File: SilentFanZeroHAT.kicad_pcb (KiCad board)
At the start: 2 copper layers, 65 x 30 mm, 43 parts, among them J1 24V Input, J2 Fan_0, J3 Fan_1, J4 Fan_2, P1 Conn_02x20_Odd_Even, Q1 AOSS32338C, Q2 AOSS32338C, Q3 AOSS32338C, U1 74LVC1G17, U2 74LVC1G17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

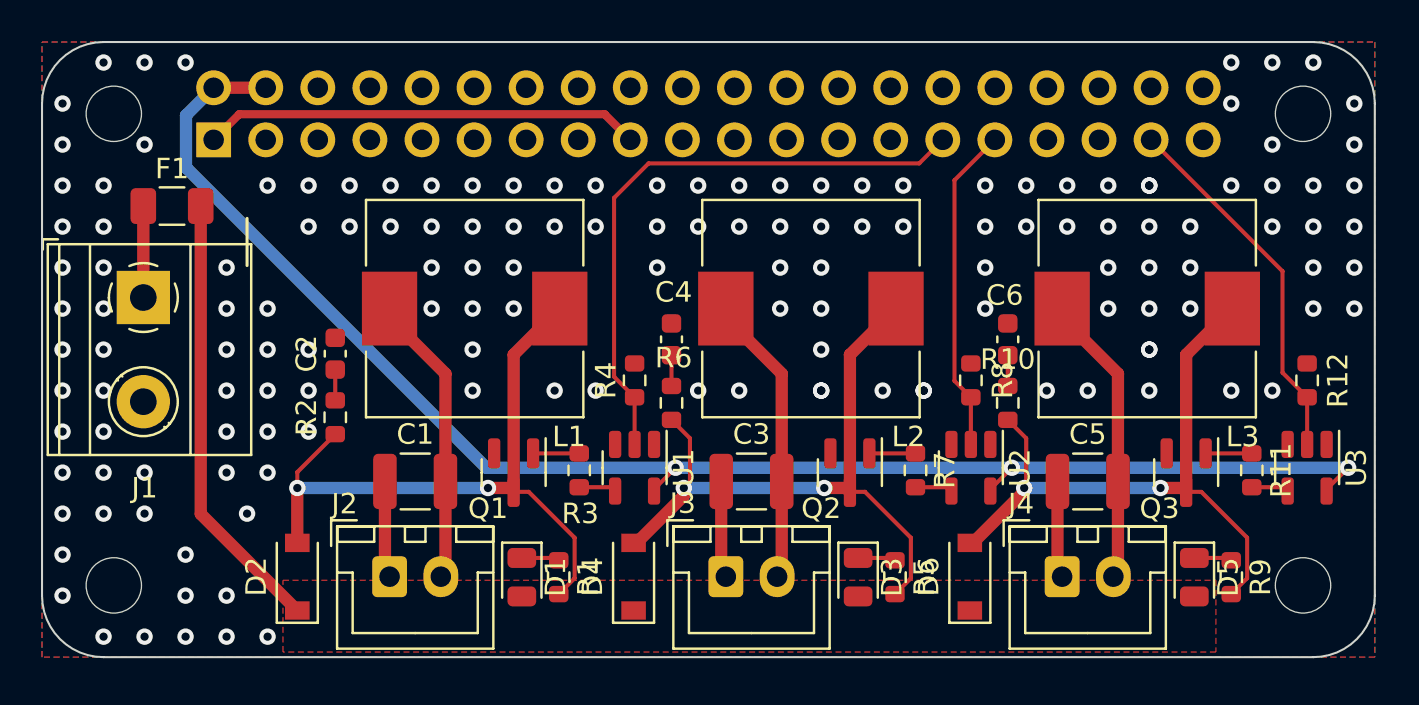
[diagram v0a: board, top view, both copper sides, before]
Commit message: Fixing the silkscreen mess
Thanks Infinite Entropy for alerting me about that.
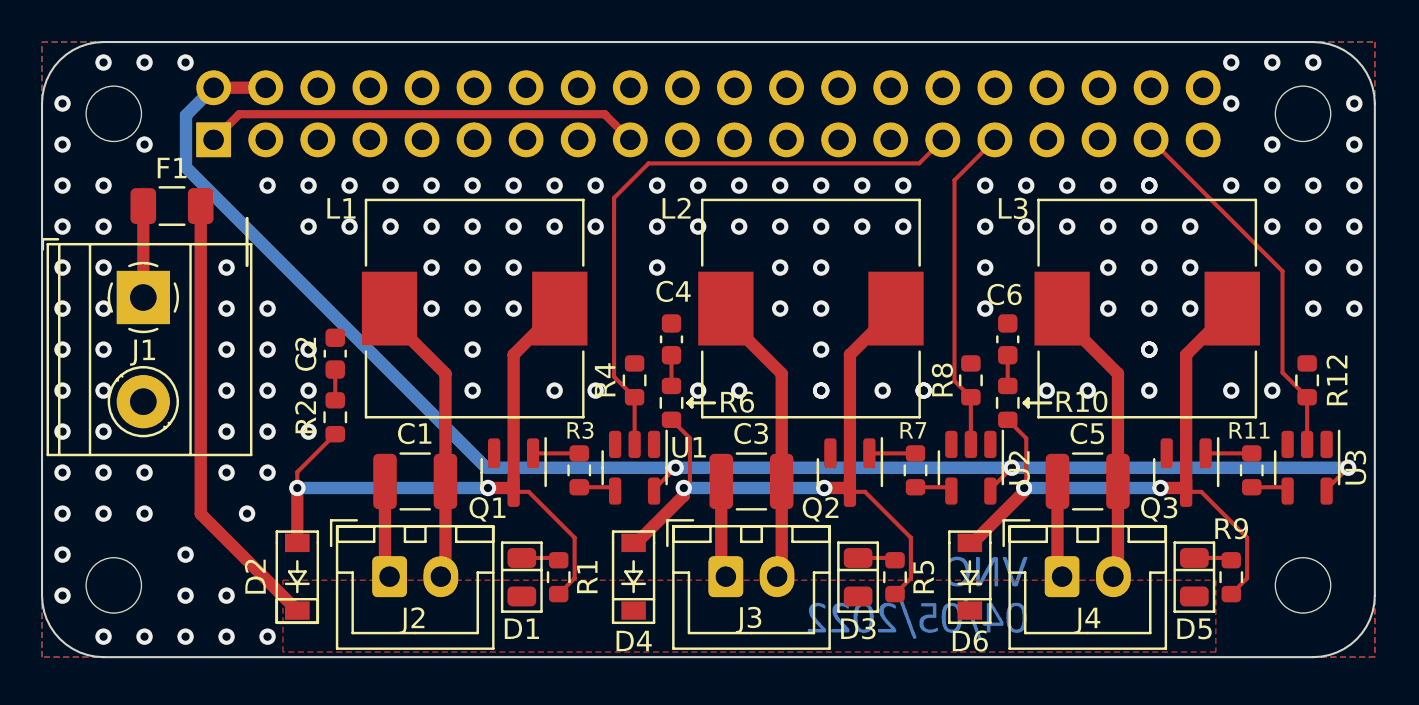
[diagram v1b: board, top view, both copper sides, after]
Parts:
- added G***: LOGO, Awesome_face:Awesome_face, B.Cu at (232.5, 109.0)
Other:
- board text added: "+"
- board text added: "-"
- board text added: "24V"
- board text added: "GND"
- board text added: "Silent Fan Zero HAT"
